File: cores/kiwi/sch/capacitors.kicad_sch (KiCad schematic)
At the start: 1 part

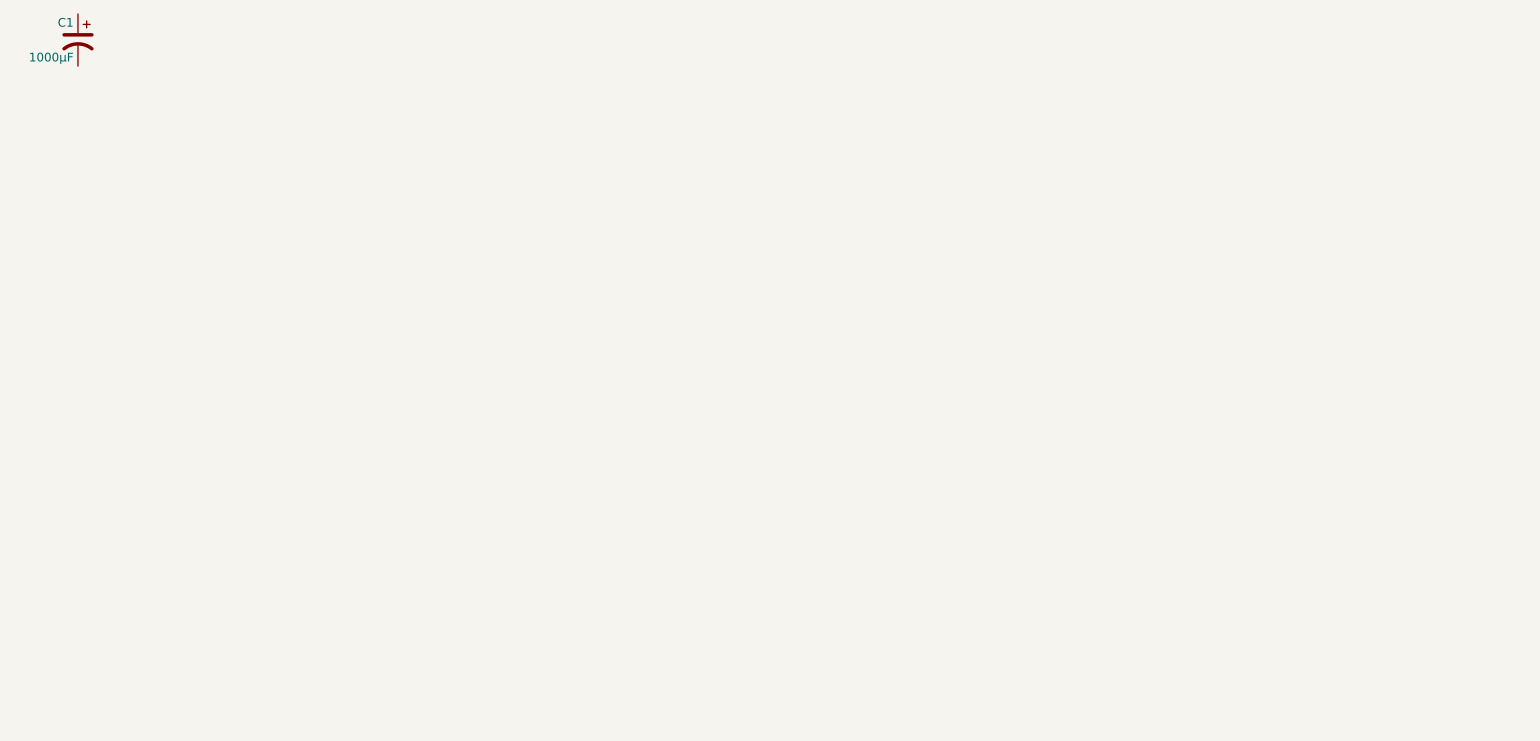
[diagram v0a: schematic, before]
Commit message: Merged sch branch. Schematics moved from extem core to kiwi core. exterm core may never be independent from the kiwi core
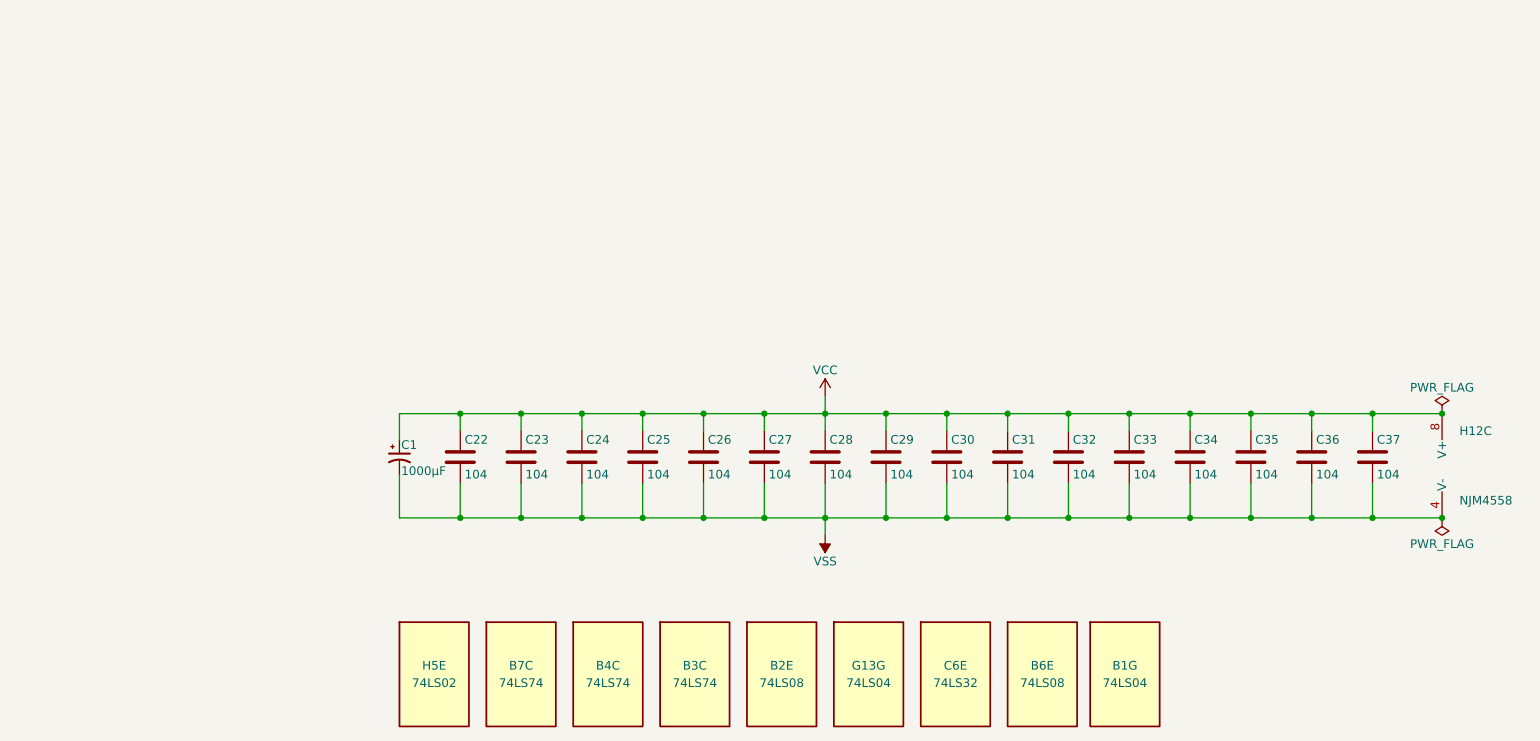
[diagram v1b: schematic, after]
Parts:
- removed C1: 1000μF, symbol Device:CP1
- added B1, G13: 74LS04, symbol jt74:74LS04
- added B2, B6: 74LS08, symbol jt74:74LS08
- added B3, B4, B7: 74LS74, symbol jt74:74LS74
- added C1: 1000μF, symbol Device:C_Polarized_Small_US
- added C22, C23, C24, C25, C26, C27, C28, C29, C30, C31, C32, C33, C34, C35, C36, C37: 104, symbol Device:C
- added C6: 74LS32, symbol jt74:74LS32
- added H12: NJM4558, symbol Amplifier_Operational:NJM4558
- added H5: 74LS02, symbol jt74:74LS02
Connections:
- new net VCC: B1.14 (VCC), B2.14 (VCC), B3.14 (VCC), B4.14 (VCC), B6.14 (VCC), B7.14 (VCC), C1.1, C22.1, C23.1, C24.1, C25.1, C26.1, C27.1, C28.1, C29.1, C30.1, C31.1, C32.1, C33.1, C34.1, C35.1, C36.1, C37.1, C6.14 (VCC), G13.14 (VCC), H12.8 (V+), H5.14 (VCC)
- new net VSS: B1.7 (VSS), B2.7 (VSS), B3.7 (VSS), B4.7 (VSS), B6.7 (VSS), B7.7 (VSS), C1.2, C22.2, C23.2, C24.2, C25.2, C26.2, C27.2, C28.2, C29.2, C30.2, C31.2, C32.2, C33.2, C34.2, C35.2, C36.2, C37.2, C6.7 (VSS), G13.7 (VSS), H12.4 (V-), H5.7 (VSS)
